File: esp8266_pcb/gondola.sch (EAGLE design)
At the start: 22 parts, among them X1 1751248, X2 1751264

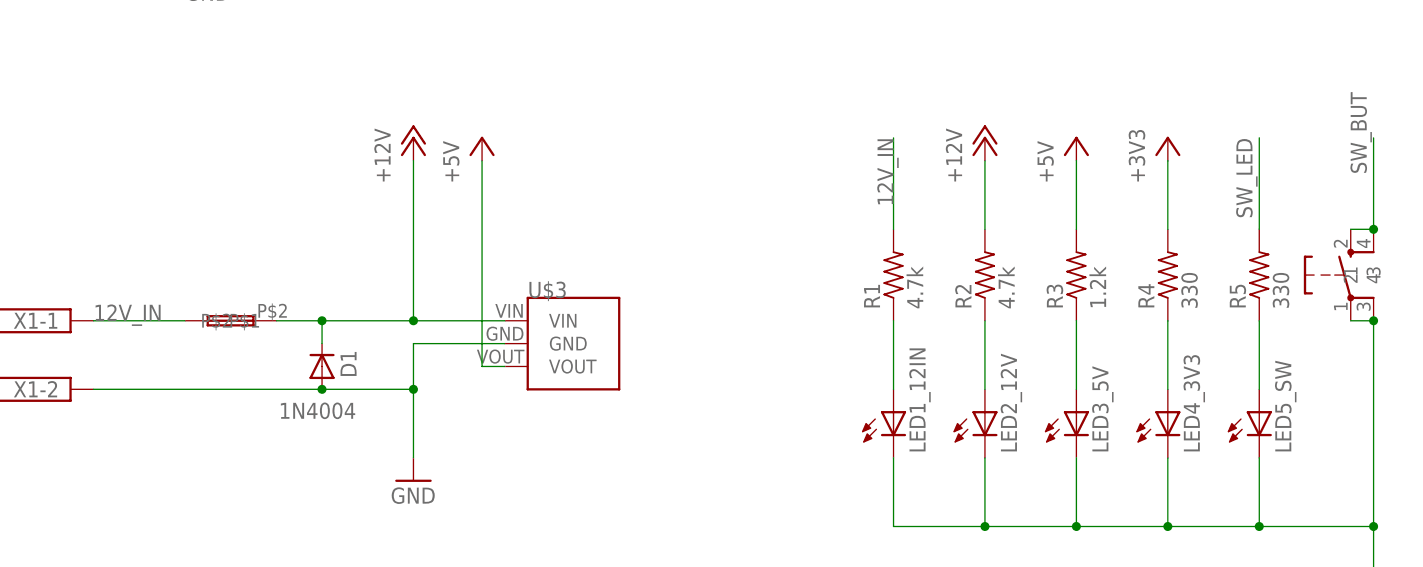
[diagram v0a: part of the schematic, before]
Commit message: deleted old layout. Corrected footbrint of button. Changed pins to Adafruit HUZZAH. Added RSSI measurements
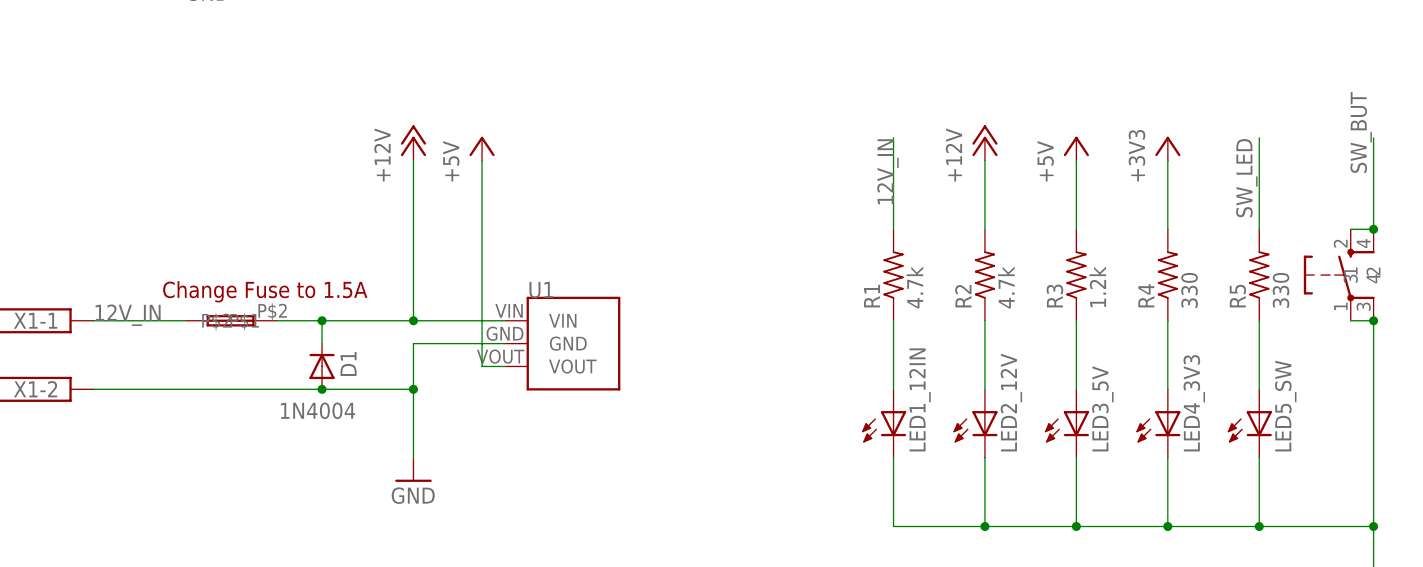
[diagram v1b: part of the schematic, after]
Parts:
- renumbered U$3 to U1
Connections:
- net GND: now also U$4.2; no longer U$4.3
- net SW_BUT: now also U$4.3; no longer U$4.2
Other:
- note added: "Change Fuse to 1.5A"
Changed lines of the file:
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@@
 <setting verticaltext="up"/>
 </settings>
-<grid distance="0.1" unitdist="inch" unit="inch" style="lines" multiple="1" display="yes" altdistance="0.01" altunitdist="inch" altunit="inch"/>
+<grid distance="0.1" unitdist="inch" unit="inch" style="lines" multiple="1" display="no" altdistance="0.01" altunitdist="inch" altunit="inch"/>
 <layers>
 <layer number="1" name="Top" color="4" fill="1" visible="no" active="no"/>
@@
 <part name="GND4" library="supply1" library_urn="urn:adsk.eagle:library:371" deviceset="GND" device=""/>
 <part name="P+2" library="supply1" library_urn="urn:adsk.eagle:library:371" deviceset="+12V" device=""/>
-<part name="U$3" library="MS" deviceset="ROHM_BP5293-XX" device=""/>
+<part name="U1" library="MS" deviceset="ROHM_BP5293-XX" device=""/>
 <part name="P+3" library="supply1" library_urn="urn:adsk.eagle:library:371" deviceset="+5V" device=""/>
 <part name="P+4" library="supply1" library_urn="urn:adsk.eagle:library:371" deviceset="+5V" device=""/>
@@
 <text x="40.64" y="27.94" size="1.778" layer="94">Don't use 0, 2 and 15</text>
 <text x="2.54" y="20.32" size="1.778" layer="94">VIN comes from FTDI cable</text>
+<text x="17.78" y="-101.6" size="1.778" layer="94">Change Fuse to 1.5A</text>
 </plain>
 <instances>
@@
 <instance part="GND4" gate="1" x="58.42" y="2.54"/>
 <instance part="P+2" gate="1" x="109.22" y="-83.82"/>
-<instance part="U$3" gate="G$1" x="66.04" y="-104.14"/>
+<instance part="U1" gate="G$1" x="66.04" y="-104.14"/>
 <instance part="P+3" gate="1" x="53.34" y="-83.82"/>
 <instance part="P+4" gate="1" x="-27.94" y="45.72"/>
@@
 <pinref part="GND1" gate="1" pin="GND"/>
 <wire x1="45.72" y1="-111.76" x2="45.72" y2="-119.38" width="0.1524" layer="91"/>
-<pinref part="U$3" gate="G$1" pin="GND"/>
+<pinref part="U1" gate="G$1" pin="GND"/>
 <wire x1="35.56" y1="-111.76" x2="45.72" y2="-111.76" width="0.1524" layer="91"/>
 <wire x1="55.88" y1="-106.68" x2="45.72" y2="-106.68" width="0.1524" layer="91"/>
@@
 <wire x1="139.7" y1="-119.38" x2="139.7" y2="-127" width="0.1524" layer="91"/>
 <junction x="139.7" y="-127"/>
+<pinref part="U$4" gate="G$1" pin="2"/>
 <wire x1="152.4" y1="-104.14" x2="152.4" y2="-127" width="0.1524" layer="91"/>
 <junction x="152.4" y="-127"/>
 <pinref part="U$4" gate="G$1" pin="1"/>
 <wire x1="149.86" y1="-104.14" x2="152.4" y2="-104.14" width="0.1524" layer="91"/>
-<pinref part="U$4" gate="G$1" pin="3"/>
 <junction x="152.4" y="-104.14"/>
 </segment>
@@
 <wire x1="35.56" y1="-104.14" x2="45.72" y2="-104.14" width="0.1524" layer="91"/>
 <wire x1="45.72" y1="-104.14" x2="45.72" y2="-86.36" width="0.1524" layer="91"/>
-<pinref part="U$3" gate="G$1" pin="VIN"/>
+<pinref part="U1" gate="G$1" pin="VIN"/>
 <wire x1="45.72" y1="-104.14" x2="55.88" y2="-104.14" width="0.1524" layer="91"/>
 <junction x="45.72" y="-104.14"/>
@@
 <net name="+5V" class="0">
 <segment>
-<pinref part="U$3" gate="G$1" pin="VOUT"/>
+<pinref part="U1" gate="G$1" pin="VOUT"/>
 <wire x1="55.88" y1="-109.22" x2="53.34" y2="-109.22" width="0.1524" layer="91"/>
 <wire x1="53.34" y1="-109.22" x2="53.34" y2="-86.36" width="0.1524" layer="91"/>
@@
 <label x="149.86" y="-78.74" size="1.778" layer="95" rot="R270"/>
 <pinref part="U$4" gate="G$1" pin="4"/>
-<pinref part="U$4" gate="G$1" pin="2"/>
+<pinref part="U$4" gate="G$1" pin="3"/>
 <wire x1="149.86" y1="-93.98" x2="152.4" y2="-93.98" width="0.1524" layer="91"/>
 <junction x="152.4" y="-93.98"/>
